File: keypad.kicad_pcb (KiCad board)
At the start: 2 copper layers, 18 x 15 mm, 15 parts

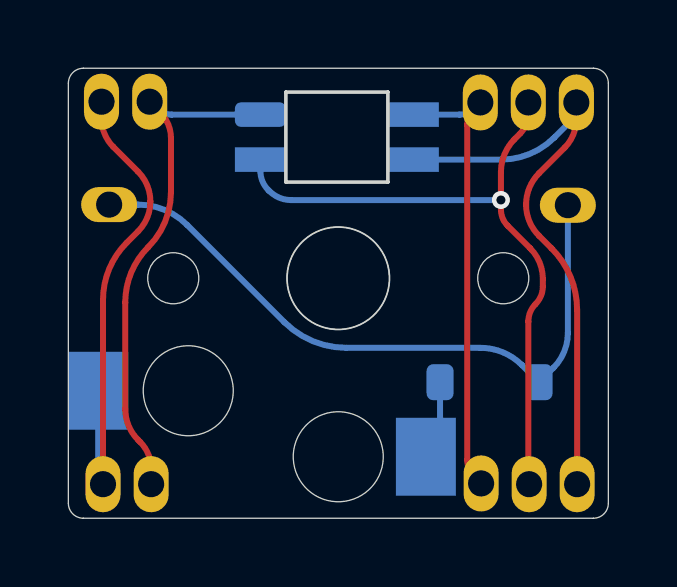
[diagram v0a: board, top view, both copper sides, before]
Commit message: Adding choc v2 support and VCC denoise cap
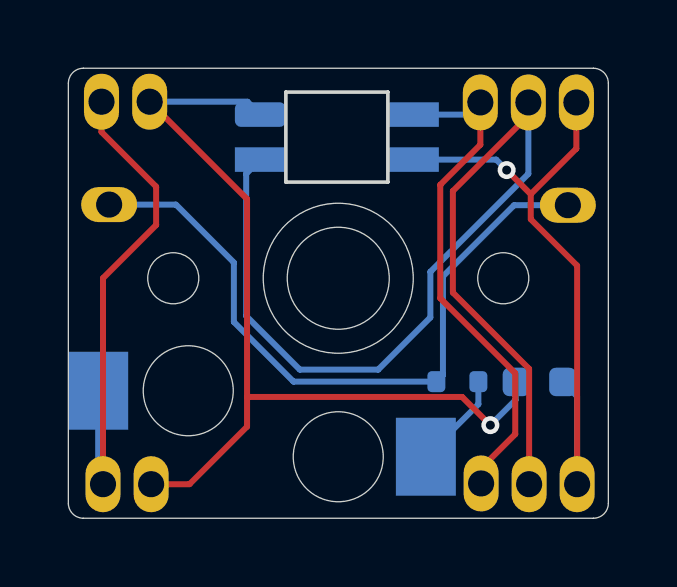
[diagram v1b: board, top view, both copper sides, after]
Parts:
- added C1: 100nF, Capacitor_SMD:C_0603_1608Metric, B.Cu at (95.1, 143.2)
- D1: footprint ScottoKeebs_Components:Diode_SOD-123 -> Diode_SMD:D_SOD-523
- moved D1 1.07 mm to (92.3, 143.2), turned to 0 degrees
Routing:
- net IN: track 23.0 -> 36.4 mm, vias 1 -> 0
- net GND: track 17.4 -> 30.3 mm, vias 0 -> 1
- net VSS: track 20.1 -> 22.0 mm, vias 0 -> 1
- net OUT: track 15.4 -> 17.2 mm
- net Net-(D1-A): track 2.64 -> 3.23 mm
- net ROW: track 22.7 -> 23.3 mm
- net COL: track 16.9 -> 17.4 mm

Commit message: BOM patches
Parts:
- D2: value LED_SK6812MINI -> SK6812-MINI-E; footprint ScottoKeebs_Components:LED_SK6812MINI -> Keebio-Parts:SK6812-MINI-E; moved to B.Cu
- turned D2 to 180 degrees
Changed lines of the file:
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@@
 		(embedded_fonts no)
-	)
-	(footprint "ScottoKeebs_Components:LED_SK6812MINI"
-		(layer "F.Cu")
-		(at 88.333337 135.038492)
-		(property "Reference" "D2"
-			(at 0 2.1 0)
-			(unlocked yes)
-			(layer "B.SilkS")
-			(hide yes)
-			(effects
-				(font
-					(size 0.7 0.7)
-					(thickness 0.15)
-				)
-				(justify mirror)
-			)
-		)
-		(property "Value" "LED_SK6812MINI"
-			(at 0 -0.5 0)
-			(unlocked yes)
-			(layer "F.SilkS")
-			(hide yes)
-			(effects
-				(font
-					(size 1 1)
-					(thickness 0.15)
-				)
-			)
-		)
-		(property "Datasheet" "https://cdn-shop.adafruit.com/product-files/2686/SK6812MINI_REV.01-1-2.pdf"
-			(at 0 0 0)
-			(layer "F.Fab")
-			(hide yes)
-			(effects
-				(font
-					(size 1.27 1.27)
-					(thickness 0.15)
-				)
-			)
-		)
-		(property "Description" "RGB LED with integrated controller"
-			(at 0 0 0)
-			(layer "F.Fab")
-			(hide yes)
-			(effects
-				(font
-					(size 1.27 1.27)
-					(thickness 0.15)
-				)
-			)
-		)
-		(property ki_fp_filters "LED*SK6812MINI*PLCC*3.5x3.5mm*P1.75mm*")
-		(sheetname "/")
-		(sheetfile "keypad.kicad_sch")
-		(attr through_hole)
-		(fp_poly
-			(pts
-				(xy -2.8 -1.4) (xy -2.2 -1.4) (xy -2.2 -2)
-			)
-			(stroke
-				(width 0.1)
-				(type solid)
-			)
-			(fill yes)
-			(layer "B.SilkS")
-		)
-		(fp_line
-			(start -1.7 -1.5)
-			(end -1.7 1.5)
-			(stroke
-				(width 0.12)
-				(type solid)
-			)
-			(layer "Edge.Cuts")
-		)
-		(fp_line
-			(start -1.7 1.5)
-			(end 1.7 1.5)
-			(stroke
-				(width 0.12)
-				(type solid)
-			)
-			(layer "Edge.Cuts")
-		)
-		(fp_line
-			(start 1.7 -1.5)
-			(end -1.7 -1.5)
-			(stroke
-				(width 0.12)
-				(type solid)
-			)
-			(layer "Edge.Cuts")
-		)
-		(fp_line
-			(start 1.7 1.5)
-			(end 1.7 -1.5)
-			(stroke
-				(width 0.12)
-				(type solid)
-			)
-			(layer "Edge.Cuts")
-		)
-		(pad "1" smd rect
-			(at 2.55 0.75)
-			(size 1.7 0.82)
-			(layers "B.Cu" "B.Mask" "B.Paste")
-			(net 4 "VSS")
-			(pinfunction "VSS")
-			(pintype "output")
-		)
-		(pad "2" smd rect
-			(at 2.55 -0.75)
-			(size 1.7 0.82)
-			(layers "B.Cu" "B.Mask" "B.Paste")
-			(net 6 "OUT")
-			(pinfunction "DOUT")
-			(pintype "power_in")
-		)
-		(pad "3" smd roundrect
-			(at -2.55 -0.75)
-			(size 1.7 0.82)
-			(layers "B.Cu" "B.Mask" "B.Paste")
-			(roundrect_rratio 0.25)
-			(net 1 "GND")
-			(pinfunction "GND")
-			(pintype "input")
-		)
-		(pad "4" smd rect
-			(at -2.55 0.75)
-			(size 1.7 0.82)
-			(layers "B.Cu" "B.Mask" "B.Paste")
-			(net 7 "IN")
-			(pinfunction "DIN")
-			(pintype "power_in")
-		)
-		(embedded_fonts no)
-		(model "${SCOTTOKEEBS_KICAD}/3dmodels/ScottoKeebs_Components.3dshapes/LED_SK6812MINI.step"
-			(offset
-				(xyz 0 0 -1.25)
-			)
-			(scale
-				(xyz 1 1 1)
-			)
-			(rotate
-				(xyz 90 180 -0)
-			)
-		)
 	)
 	(footprint ""
@@
 			)
 		)
+		(property "LCSC" "C83482"
+			(at 0 0 0)
+			(unlocked yes)
+			(layer "B.Fab")
+			(hide yes)
+			(effects
+				(font
+					(size 1 1)
+					(thickness 0.15)
+				)
+				(justify mirror)
+			)
+		)
 		(property ki_fp_filters "D*DO?35*")
 		(sheetname "/")
@@
 			)
 		)
-		(property "Datasheet" ""
+		(property "Datasheet" "~"
 			(at 0 0 0)
 			(layer "B.Fab")
@@
 			)
 		)
-		(property "LCSC" "C1525"
+		(property "LCSC" "C14663"
 			(at 0 0 0)
 			(unlocked yes)
@@
 			)
 		)
+	)
+	(footprint "Keebio-Parts:SK6812-MINI-E"
+		(layer "B.Cu")
+		(at 88.333337 135.038492 180)
+		(property "Reference" "D2"
+			(at 0 -2.1 0)
+			(unlocked yes)
+			(layer "B.SilkS")
+			(hide yes)
+			(effects
+				(font
+					(size 0.7 0.7)
+					(thickness 0.15)
+				)
+				(justify mirror)
+			)
+		)
+		(property "Value" "SK6812-MINI-E"
+			(at 0 0.5 0)
+			(unlocked yes)
+			(layer "B.SilkS")
+			(hide yes)
+			(effects
+				(font
+					(size 1 1)
+					(thickness 0.15)
+				)
+				(justify mirror)
+			)
+		)
+		(property "Datasheet" ""
+			(at 0 0 0)
+			(layer "B.Fab")
+			(hide yes)
+			(effects
+				(font
+					(size 1.27 1.27)
+					(thickness 0.15)
+				)
+				(justify mirror)
+			)
+		)
+		(property "Description" ""
+			(at 0 0 0)
+			(layer "B.Fab")
+			(hide yes)
+			(effects
+				(font
+					(size 1.27 1.27)
+					(thickness 0.15)
+				)
+				(justify mirror)
+			)
+		)
+		(property "LCSC" "C5149201"
+			(at 0 0 0)
+			(unlocked yes)
+			(layer "B.Fab")
+			(hide yes)
+			(effects
+				(font
+					(size 1 1)
+					(thickness 0.15)
+				)
+				(justify mirror)
+			)
+		)
+		(property ki_fp_filters "LED*SK6812MINI*PLCC*3.5x3.5mm*P1.75mm*")
+		(sheetname "/")
+		(sheetfile "keypad.kicad_sch")
+		(attr through_hole)
+		(fp_poly
+			(pts
+				(xy 2.8 1.4) (xy 2.2 1.4) (xy 2.2 2)
+			)
+			(stroke
+				(width 0.1)
+				(type solid)
+			)
+			(fill yes)
+			(layer "B.SilkS")
+		)
+		(fp_line
+			(start 1.7 1.5)
+			(end 1.7 -1.5)
+			(stroke
+				(width 0.12)
+				(type solid)
+			)
+			(layer "Edge.Cuts")
+		)
+		(fp_line
+			(start 1.7 -1.5)
+			(end -1.7 -1.5)
+			(stroke
+				(width 0.12)
+				(type solid)
+			)
+			(layer "Edge.Cuts")
+		)
+		(fp_line
+			(start -1.7 1.5)
+			(end 1.7 1.5)
+			(stroke
+				(width 0.12)
+				(type solid)
+			)
+			(layer "Edge.Cuts")
+		)
+		(fp_line
+			(start -1.7 -1.5)
+			(end -1.7 1.5)
+			(stroke
+				(width 0.12)
+				(type solid)
+			)
+			(layer "Edge.Cuts")
+		)
+		(pad "1" smd rect
+			(at -2.55 -0.75 180)
+			(size 1.7 0.82)
+			(layers "B.Cu" "B.Mask" "B.Paste")
+			(net 4 "VSS")
+			(pinfunction "VSS")
+			(pintype "output")
+		)
+		(pad "2" smd rect
+			(at -2.55 0.75 180)
+			(size 1.7 0.82)
+			(layers "B.Cu" "B.Mask" "B.Paste")
+			(net 6 "OUT")
+			(pinfunction "DOUT")
+			(pintype "power_in")
+		)
+		(pad "3" smd roundrect
+			(at 2.55 0.75 180)
+			(size 1.7 0.82)
+			(layers "B.Cu" "B.Mask" "B.Paste")
+			(roundrect_rratio 0.25)
+			(net 1 "GND")
+			(pinfunction "GND")
+			(pintype "input")
+		)
+		(pad "4" smd rect
+			(at 2.55 -0.75 180)
+			(size 1.7 0.82)
+			(layers "B.Cu" "B.Mask" "B.Paste")
+			(net 7 "IN")
+			(pinfunction "DIN")
+			(pintype "power_in")
+		)
+		(embedded_fonts no)
+		(model "${SCOTTOKEEBS}/3dmodels/ScottoKeebs_Components.3dshapes/LED_SK6812MINI.step"
+			(offset
+				(xyz 0 0 0)
+			)
+			(scale
+				(xyz 1 1 1)
+			)
+			(rotate
+				(xyz 90 0 0)
+			)
+		)

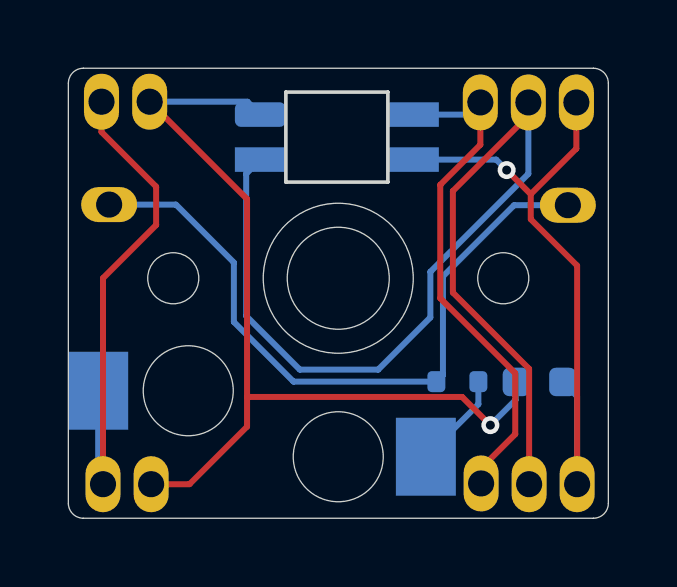
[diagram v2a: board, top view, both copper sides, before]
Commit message: Swapping the socket model
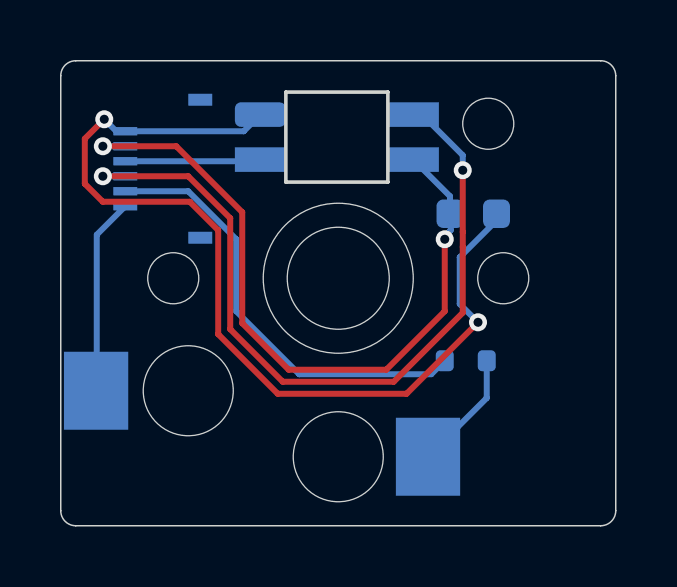
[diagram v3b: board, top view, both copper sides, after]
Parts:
- removed ? (x12): , 
- added J1: Conn_01x06_MountingPin, Hirose_FH19C-6S-0.5SH_1x06:Hirose_FH19C-6S-0.5SH_1x06, B.Cu at (82.5, 136.1)
- D2: value SK6812-MINI-E -> LED_SK6812MINI
- moved C1 6.02 mm to (92.9, 137.6), turned to 0 degrees
- moved D1 0.75 mm to (92.6, 142.5)
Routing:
- net IN: track 36.4 -> 4.53 mm
- net COL: track 17.4 -> 6.55 mm
- net OUT: track 17.2 -> 26.4 mm, vias 0 -> 2
- net ROW: track 23.3 -> 14.8 mm
- net VSS: track 22.0 -> 23.9 mm, vias 1 -> 2
- net GND: track 30.3 -> 31.4 mm, vias 1 -> 2
- net Net-(D1-A): track 3.23 -> 4.01 mm
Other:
- board size 18 x 15 mm -> 18.5 x 15.5 mm
- board text removed: "col"
- board text removed: "gnd"
- board text removed: "in"
- board text removed: "out"
- board text removed: "row"
- board text removed: "vcc"
